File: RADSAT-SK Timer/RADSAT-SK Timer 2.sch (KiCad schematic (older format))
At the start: 34 parts, among them J201 Conn_01x07, J202 Conn_01x05, J203 Conn_01x02, J204 Conn_01x02, J204 USB_B_Micro, J205 Conn_01x02, J206 Conn_01x02, Q201 IRLML2060, SW201 SW_Push, SW202 SW_Push, SW203 SW_Push, SW204 SW_Push, SW205 SW_Push, SW206 SW_Push, U202 LTC3440EMSPBF

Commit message: 1.Added USB Header, Footprint and lib files 2. got rid of the rescue library by reassigning the symbols to proper libraries in the project 3. assigned footprints to all components, though BOM still MIA. Diode MBRM appears to be discontinues on digikey???
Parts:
- removed J204: USB_B_Micro, Connector_USB:USB_Micro-B_Molex-105133-0001, symbol RADSAT-SK-Timer-rescue:USB_B_Micro-Connector-RADSAT-SK-Timer-rescue
- added J210: ZX62WRD-B-5PC, ZX62WRD-B-5PC:ZX62WRD-B-5PC, symbol ZX62WRD-B-5PC:ZX62WRD-B-5PC
- D201: footprint (none) -> Diode_SMD:D_0805_2012Metric
- D203: symbol RADSAT-SK-Timer-rescue:MBR1020VL-Diode-RADSAT-SK-Timer-rescue -> Diode:MBR1020VL
- J201: footprint (none) -> Connector_Molex:Molex_PicoBlade_53047-0710_1x07_P1.25mm_Vertical
- J202: footprint (none) -> Connector_Hirose:Hirose_DF13-05P-1.25DSA_1x05_P1.25mm_Vertical
- Q201: symbol RADSAT-SK-Timer-rescue:IRLML2060-Transistor_FET-RADSAT-SK-Timer-rescue -> Transistor_FET:IRLML2060
- R220, R221: footprint (none) -> Resistor_SMD:R_0805_2012Metric
- SW201: footprint Connector_Hirose:Hirose_DF13-02P-1.25DSA_1x02_P1.25mm_Vertical -> Connector_Hirose:Hirose_DF11-30DP-2DSA_2x15_P2.00mm_Vertical
- U202: symbol RADSAT-SK-Timer-rescue:LTC3440EMSPBF-LTC3440EMSPBF-RADSAT-SK-Timer-rescue -> LTC3440EMSPBF:LTC3440EMSPBF
- gave numbers to parts that had none: 3
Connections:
- net +5V: now also D205.2 (A), J204.1 (Pin_1), J205.1 (Pin_1), J206.1 (Pin_1)
- net +BATT: now also D204.2 (A)
- net GND: now also J203.2 (Pin_2), J204.2 (Pin_2), J205.2 (Pin_2), J206.2 (Pin_2), J210.5
- net USB_Charge: now also J210.1
- net at J203.1 (Pin_1): now also D204.1 (K), D205.1 (K)
- no-connect marks 5 -> 4
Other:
- note added: "RBF Logic for Batt Board Inhibit"
- moved on the sheet: D204, D205, J203
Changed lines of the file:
@@
 $EndComp
 $Comp
-L RADSAT-SK-Timer-rescue:LTC3440EMSPBF-LTC3440EMSPBF-RADSAT-SK-Timer-rescue U202
+L LTC3440EMSPBF:LTC3440EMSPBF U202
 U 1 1 6019F249
 P 8400 2100
@@
 $EndComp
 $Comp
-L RADSAT-SK-Timer-rescue:IRLML2060-Transistor_FET-RADSAT-SK-Timer-rescue Q201
+L Transistor_FET:IRLML2060 Q201
 U 1 1 600FFF1C
 P 7000 2500
@@
 	6300 2025 6300 1850
 $Comp
-L RADSAT-SK-Timer-rescue:MBR1020VL-Diode-RADSAT-SK-Timer-rescue D203
+L Diode:MBR1020VL D203
 U 1 1 60121A1E
 P 9400 1425
@@
 Electrical Inhibits Logic and Outputs
 Wire Wire Line
-	3475 6650 3475 6850
-Wire Wire Line
 	4825 2625 4825 2800
-Wire Wire Line
-	3475 6850 3800 6850
-Wire Wire Line
-	3800 6850 3800 6800
 $Comp
 L power:+5V #PWR0105
 U 1 1 6017CE3E
-P 3800 6800
-F 0 "#PWR0105" H 3800 6650 50  0001 C CNN
-F 1 "+5V" H 3815 6973 50  0000 C CNN
-F 2 "" H 3800 6800 50  0001 C CNN
-F 3 "" H 3800 6800 50  0001 C CNN
-	1    3800 6800
-	1    0    0    -1
+P 3475 7050
+F 0 "#PWR0105" H 3475 6900 50  0001 C CNN
+F 1 "+5V" V 3490 7223 50  0000 C CNN
+F 2 "" H 3475 7050 50  0001 C CNN
+F 3 "" H 3475 7050 50  0001 C CNN
+	1    3475 7050
+	0    -1   -1   0
 $EndComp
 $Comp
@@
 F 0 "SW201" V 4529 1973 50  0000 L CNN
 F 1 "SW_Push" V 4620 1973 50  0000 L CNN
-F 2 "Connector_Hirose:Hirose_DF13-02P-1.25DSA_1x02_P1.25mm_Vertical" H 4575 2025 50  0001 C CNN
+F 2 "Connector_Hirose:Hirose_DF11-30DP-2DSA_2x15_P2.00mm_Vertical" H 4575 2025 50  0001 C CNN
 F 3 "~" H 4575 2025 50  0001 C CNN
 	1    4575 1825
@@
 Wire Wire Line
 	4800 4150 5000 4150
-$Comp
-L RADSAT-SK-Timer-rescue:USB_B_Micro-Connector-RADSAT-SK-Timer-rescue J204
-U 1 1 60C6CBAB
-P 925 5600
-AR Path="/60C6CBAB" Ref="J204"  Part="1"
-AR Path="/602E25D3/60C6CBAB" Ref="J222"  Part="1"
-F 0 "J222" H 980 6067 50  0000 C CNN
-F 1 "USB_B_Micro" H 980 5976 50  0000 C CNN
-F 2 "Connector_USB:USB_Micro-B_Molex-105133-0001" H 1075 5550 50  0001 C CNN
-F 3 "~" H 1075 5550 50  0001 C CNN
-	1    925  5600
-	1    0    0    -1
-$EndComp
-NoConn ~ 825  6000
-NoConn ~ 1225 5800
-NoConn ~ 1225 5600
-NoConn ~ 1225 5700
-Text GLabel 1350 5400 2    50   Input ~ 0
+NoConn ~ 1150 5800
+NoConn ~ 1150 5600
+NoConn ~ 1150 5700
+Text GLabel 1375 5500 2    50   Input ~ 0
 USB_Charge
-Wire Wire Line
-	1350 5400 1225 5400
-$Comp
-L power:GND #PWR?
+$Comp
+L power:GND #PWR0106
 U 1 1 61514573
-P 925 6000
-F 0 "#PWR?" H 925 5750 50  0001 C CNN
-F 1 "GND" H 930 5827 50  0000 C CNN
-F 2 "" H 925 6000 50  0001 C CNN
-F 3 "" H 925 6000 50  0001 C CNN
-	1    925  6000
+P 1300 6025
+F 0 "#PWR0106" H 1300 5775 50  0001 C CNN
+F 1 "GND" H 1305 5852 50  0000 C CNN
+F 2 "" H 1300 6025 50  0001 C CNN
+F 3 "" H 1300 6025 50  0001 C CNN
+	1    1300 6025
 	1    0    0    -1
 $EndComp
@@
 F 0 "J201" H 2080 7117 50  0000 L CNN
 F 1 "Conn_01x07" H 2080 7026 50  0000 L CNN
-F 2 "" H 2000 7075 50  0001 C CNN
+F 2 "Connector_Molex:Molex_PicoBlade_53047-0710_1x07_P1.25mm_Vertical" H 2000 7075 50  0001 C CNN
 F 3 "~" H 2000 7075 50  0001 C CNN
 	1    2000 7075
@@
 L Connector_Generic:Conn_01x02 J203
 U 1 1 615188F9
-P 8350 3875
-F 0 "J203" H 8430 3867 50  0000 L CNN
-F 1 "Conn_01x02" H 8430 3776 50  0000 L CNN
-F 2 "Connector_Hirose:Hirose_DF13-02P-1.25DSA_1x02_P1.25mm_Vertical" H 8350 3875 50  0001 C CNN
-F 3 "~" H 8350 3875 50  0001 C CNN
-	1    8350 3875
+P 4300 5525
+F 0 "J203" H 4380 5517 50  0000 L CNN
+F 1 "Conn_01x02" H 4380 5426 50  0000 L CNN
+F 2 "Connector_Hirose:Hirose_DF13-02P-1.25DSA_1x02_P1.25mm_Vertical" H 4300 5525 50  0001 C CNN
+F 3 "~" H 4300 5525 50  0001 C CNN
+	1    4300 5525
 	1    0    0    -1
 $EndComp
@@
 F 0 "J202" H 2543 3075 50  0000 C CNN
 F 1 "Conn_01x05" H 2543 3166 50  0000 C CNN
-F 2 "" H 2625 3500 50  0001 C CNN
+F 2 "Connector_Hirose:Hirose_DF13-05P-1.25DSA_1x05_P1.25mm_Vertical" H 2625 3500 50  0001 C CNN
 F 3 "~" H 2625 3500 50  0001 C CNN
 	1    2625 3500
@@
 Wire Wire Line
 	1675 7375 1675 7500
-Text Notes 500  5100 0    50   ~ 0
+Text Notes 500  5125 0    50   ~ 0
 USB Charger for Battery
 Wire Notes Line
@@
 P 4700 3700
 AR Path="/6156AA9A" Ref="Q?"  Part="1"
-AR Path="/602E25D3/6156AA9A" Ref="Q?"  Part="1"
-F 0 "Q?" H 4475 3625 50  0000 L CNN
+AR Path="/602E25D3/6156AA9A" Ref="Q202"  Part="1"
+F 0 "Q202" H 4475 3625 50  0000 L CNN
 F 1 "IRLML2060" H 4375 3525 50  0000 L CNN
 F 2 "Package_TO_SOT_SMD:SOT-23" H 4900 3625 50  0001 L CIN
@@
 F 0 "R221" V 3918 3700 50  0000 C CNN
 F 1 "100" V 4009 3700 50  0000 C CNN
-F 2 "" V 4055 3700 50  0001 C CNN
+F 2 "Resistor_SMD:R_0805_2012Metric" V 4055 3700 50  0001 C CNN
 F 3 "~" H 4125 3700 50  0001 C CNN
 	1    4125 3700
@@
 F 0 "R220" H 3295 4021 50  0000 L CNN
 F 1 "300k" H 3295 3930 50  0000 L CNN
-F 2 "" V 3155 3975 50  0001 C CNN
+F 2 "Resistor_SMD:R_0805_2012Metric" V 3155 3975 50  0001 C CNN
 F 3 "~" H 3225 3975 50  0001 C CNN
 	1    3225 3975
@@
 F 0 "D201" V 3529 4055 50  0000 L CNN
 F 1 "D_Zener" V 3620 4055 50  0000 L CNN
-F 2 "" H 3575 3975 50  0001 C CNN
+F 2 "Diode_SMD:D_0805_2012Metric" H 3575 3975 50  0001 C CNN
 F 3 "~" H 3575 3975 50  0001 C CNN
 	1    3575 3975
@@
 	3400 4125 3225 4125
 $Comp
-L power:GND #PWR?
+L power:GND #PWR0108
 U 1 1 61592A30
 P 3400 4300
-F 0 "#PWR?" H 3400 4050 50  0001 C CNN
+F 0 "#PWR0108" H 3400 4050 50  0001 C CNN
 F 1 "GND" H 3405 4127 50  0000 C CNN
 F 2 "" H 3400 4300 50  0001 C CNN
@@
 	2950 3300 2825 3300
 $Comp
-L Device:D D?
+L Device:D D204
 U 1 1 615B7582
-P 6925 3725
-F 0 "D?" H 6925 3508 50  0000 C CNN
-F 1 "D" H 6925 3599 50  0000 C CNN
-F 2 "Diode_SMD:D_0805_2012Metric" H 6925 3725 50  0001 C CNN
-F 3 "~" H 6925 3725 50  0001 C CNN
-	1    6925 3725
+P 2875 5425
+F 0 "D204" H 2875 5208 50  0000 C CNN
+F 1 "D" H 2875 5299 50  0000 C CNN
+F 2 "Diode_SMD:D_0805_2012Metric" H 2875 5425 50  0001 C CNN
+F 3 "~" H 2875 5425 50  0001 C CNN
+	1    2875 5425
 	-1   0    0    1
 $EndComp
 $Comp
-L Device:D D?
+L Device:D D205
 U 1 1 615BB367
-P 6925 4000
-F 0 "D?" H 6925 3783 50  0000 C CNN
-F 1 "D" H 6925 3874 50  0000 C CNN
-F 2 "Diode_SMD:D_0805_2012Metric" H 6925 4000 50  0001 C CNN
-F 3 "~" H 6925 4000 50  0001 C CNN
-	1    6925 4000
+P 2875 5700
+F 0 "D205" H 2875 5825 50  0000 C CNN
+F 1 "D" H 2875 5900 50  0000 C CNN
+F 2 "Diode_SMD:D_0805_2012Metric" H 2875 5700 50  0001 C CNN
+F 3 "~" H 2875 5700 50  0001 C CNN
+	1    2875 5700
 	-1   0    0    1
 $EndComp
+$Comp
+L power:+BATT #PWR0116
+U 1 1 6152A0B5
+P 2375 5425
+F 0 "#PWR0116" H 2375 5275 50  0001 C CNN
+F 1 "+BATT" V 2475 5450 50  0000 C CNN
+F 2 "" H 2375 5425 50  0001 C CNN
+F 3 "" H 2375 5425 50  0001 C CNN
+	1    2375 5425
+	0    -1   -1   0
+$EndComp
+$Comp
+L power:+5V #PWR0117
+U 1 1 6152ECEE
+P 2350 5700
+F 0 "#PWR0117" H 2350 5550 50  0001 C CNN
+F 1 "+5V" V 2450 5700 50  0000 C CNN
+F 2 "" H 2350 5700 50  0001 C CNN
+F 3 "" H 2350 5700 50  0001 C CNN
+	1    2350 5700
+	0    -1   -1   0
+$EndComp
+Wire Wire Line
+	3025 5700 3125 5700
+Wire Wire Line
+	3125 5425 3025 5425
+Wire Wire Line
+	2725 5700 2350 5700
+Wire Wire Line
+	2375 5425 2725 5425
+Wire Wire Line
+	3700 6650 3700 6975
+Wire Wire Line
+	3700 7050 3475 7050
+Wire Wire Line
+	3475 6650 3700 6650
+$Comp
+L power:GND #PWR0118
+U 1 1 61553721
+P 4450 7525
+F 0 "#PWR0118" H 4450 7275 50  0001 C CNN
+F 1 "GND" H 4455 7352 50  0000 C CNN
+F 2 "" H 4450 7525 50  0001 C CNN
+F 3 "" H 4450 7525 50  0001 C CNN
+	1    4450 7525
+	1    0    0    -1
+$EndComp
+$Comp
+L power:GND #PWR0119
+U 1 1 61557785
+P 3900 5800
+F 0 "#PWR0119" H 3900 5550 50  0001 C CNN
+F 1 "GND" H 3905 5627 50  0000 C CNN
+F 2 "" H 3900 5800 50  0001 C CNN
+F 3 "" H 3900 5800 50  0001 C CNN
+	1    3900 5800
+	1    0    0    -1
+$EndComp
+Wire Wire Line
+	5475 6500 4625 6500
+Wire Wire Line
+	4625 7475 5475 7475
+Wire Wire Line
+	4625 6500 4625 6975
+Wire Wire Line
+	5475 7000 4625 7000
+Connection ~ 4625 7000
+Wire Wire Line
+	4625 7000 4625 7475
+Wire Wire Line
+	3700 6975 4625 6975
+Connection ~ 3700 6975
+Wire Wire Line
+	3700 6975 3700 7050
+Connection ~ 4625 6975
+Wire Wire Line
+	4625 6975 4625 7000
+Wire Wire Line
+	4450 7525 4525 7525
+Wire Wire Line
+	5475 7525 5475 7575
+Wire Wire Line
+	4525 7525 4525 7300
+Wire Wire Line
+	4525 7300 4800 7300
+Wire Wire Line
+	4800 6600 5475 6600
+Connection ~ 4525 7525
+Wire Wire Line
+	4525 7525 5475 7525
+Wire Wire Line
+	4800 7300 4800 7100
+Wire Wire Line
+	5475 7100 4800 7100
+Connection ~ 4800 7100
+Wire Wire Line
+	4800 7100 4800 6600
+Text Notes 2175 5125 0    50   ~ 0
+RBF Logic for Batt Board Inhibit
+Wire Wire Line
+	3125 5425 3125 5525
+Wire Wire Line
+	3900 5800 3900 5625
+Wire Wire Line
+	3900 5625 4100 5625
+Wire Wire Line
+	4100 5525 3125 5525
+Connection ~ 3125 5525
+Wire Wire Line
+	3125 5525 3125 5700
+Wire Notes Line
+	4925 5000 4925 6300
+$Comp
+L ZX62WRD-B-5PC:ZX62WRD-B-5PC J210
+U 1 1 6159DCFD
+P 1150 5500
+F 0 "J210" H 1392 5787 60  0000 C CNN
+F 1 "ZX62WRD-B-5PC" H 1392 5681 60  0000 C CNN
+F 2 "ZX62WRD-B-5PC:ZX62WRD-B-5PC" H 1550 5240 60  0001 C CNN
+F 3 "https://www.digikey.ca/en/products/detail/hirose-electric-co-ltd/ZX62WRD-B-5PC/3761053" H 1150 5500 60  0001 C CNN
+	1    1150 5500
+	-1   0    0    -1
+$EndComp
+Wire Wire Line
+	1150 5500 1375 5500
+Wire Wire Line
+	1150 5900 1300 5900
+Wire Wire Line
+	1300 5900 1300 6025
 $EndSCHEMATC

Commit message: PCBheader layout version 1, Note Main Bus Headers are on back of PCB to line pin 1 with batt board, RBF output is 3pin??? Need proper allignment of Main header
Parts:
- SW201: footprint Connector_Hirose:Hirose_DF11-30DP-2DSA_2x15_P2.00mm_Vertical -> Connector_Hirose:Hirose_DF13-02P-1.25DSA_1x02_P1.25mm_Vertical
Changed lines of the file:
@@
 F 0 "SW201" V 4529 1973 50  0000 L CNN
 F 1 "SW_Push" V 4620 1973 50  0000 L CNN
-F 2 "Connector_Hirose:Hirose_DF11-30DP-2DSA_2x15_P2.00mm_Vertical" H 4575 2025 50  0001 C CNN
+F 2 "Connector_Hirose:Hirose_DF13-02P-1.25DSA_1x02_P1.25mm_Vertical" H 4575 2025 50  0001 C CNN
 F 3 "~" H 4575 2025 50  0001 C CNN
 	1    4575 1825

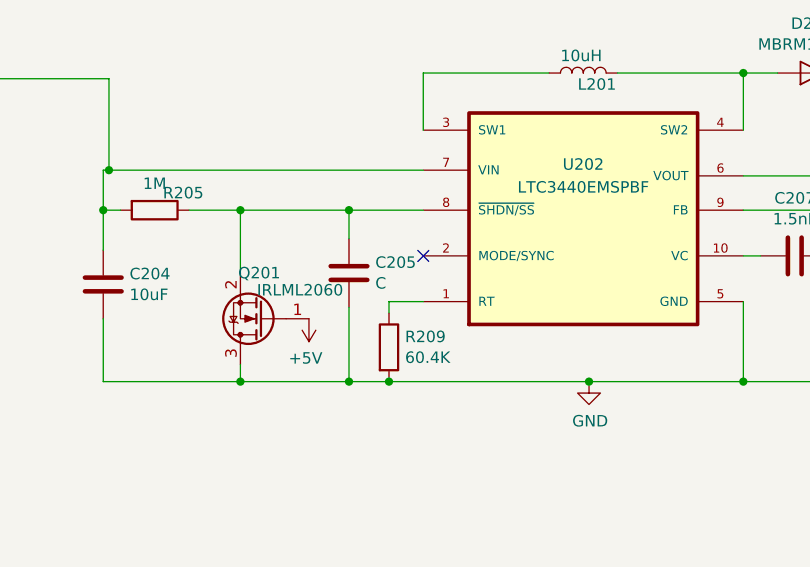
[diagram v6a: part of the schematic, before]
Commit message: Added missing Capacitor value from old schematic in the slack discussion
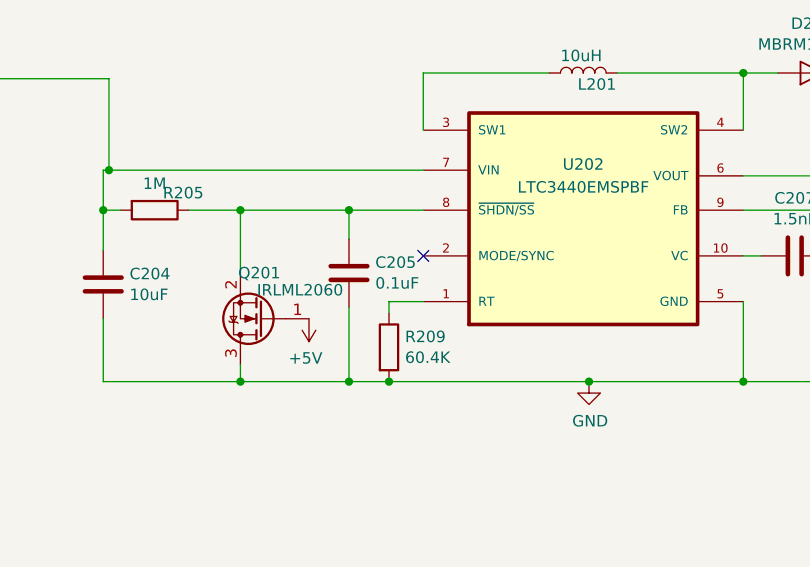
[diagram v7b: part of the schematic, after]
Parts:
- C205: value C -> 0.1uF
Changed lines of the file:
@@
 P 7375 2300
 F 0 "C205" H 7490 2346 50  0000 L CNN
-F 1 "C" H 7490 2255 50  0000 L CNN
+F 1 "0.1uF" H 7490 2255 50  0000 L CNN
 F 2 "Capacitor_SMD:C_0805_2012Metric" H 7413 2150 50  0001 C CNN
 F 3 "~" H 7375 2300 50  0001 C CNN

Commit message: Cleaned Up the USb footprint and updated the libraries to play nice with KiCad
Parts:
- J210: footprint ZX62WRD-B-5PC:ZX62WRD-B-5PC -> CONN_ZX62WRD-B-5PC_HIR:CONN_ZX62WRD-B-5PC_HIR; symbol ZX62WRD-B-5PC:ZX62WRD-B-5PC -> CONN_ZX62WRD-B-5PC_HIR:ZX62WRD-B-5PC
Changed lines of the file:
@@
 	4925 5000 4925 6300
 $Comp
-L ZX62WRD-B-5PC:ZX62WRD-B-5PC J210
+L CONN_ZX62WRD-B-5PC_HIR:ZX62WRD-B-5PC J210
 U 1 1 6159DCFD
 P 1150 5500
+AR Path="/6159DCFD" Ref="J210"  Part="1"
+AR Path="/602E25D3/6159DCFD" Ref="J210"  Part="1"
 F 0 "J210" H 1392 5787 60  0000 C CNN
 F 1 "ZX62WRD-B-5PC" H 1392 5681 60  0000 C CNN
-F 2 "ZX62WRD-B-5PC:ZX62WRD-B-5PC" H 1550 5240 60  0001 C CNN
+F 2 "CONN_ZX62WRD-B-5PC_HIR:CONN_ZX62WRD-B-5PC_HIR" H 1550 5240 60  0001 C CNN
 F 3 "https://www.digikey.ca/en/products/detail/hirose-electric-co-ltd/ZX62WRD-B-5PC/3761053" H 1150 5500 60  0001 C CNN
 	1    1150 5500
